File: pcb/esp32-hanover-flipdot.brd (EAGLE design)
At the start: 45.1 x 25.4 mm, 28 parts, among them J1 DC-005, J2 HANOVER, J3 FTDI, Q1 NCE3407A, Q2 S9013, U1 ESP32-PICO-D4, U2 CJA1117B-3.3-SOT89, U3 LM2576SX-5.0/NOPB

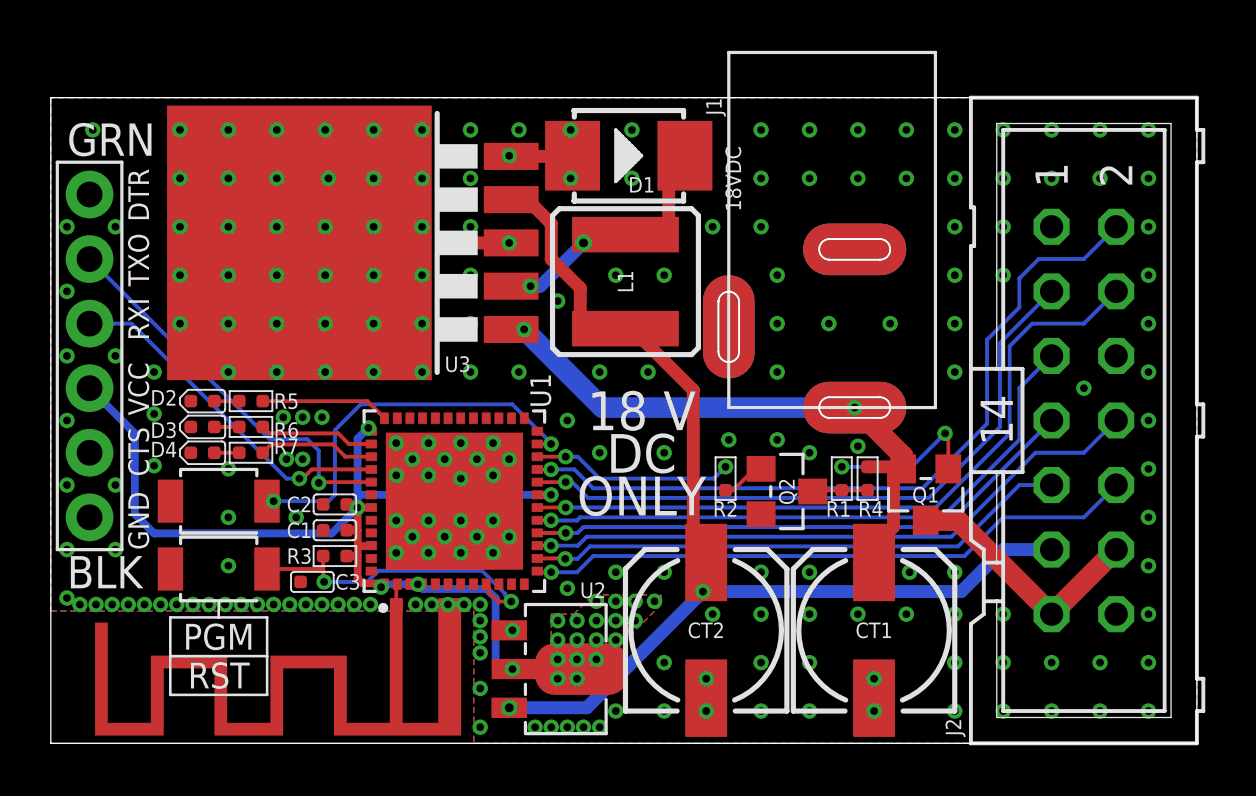
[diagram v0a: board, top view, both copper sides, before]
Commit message: pcb: Connect dot board pin 14 to COIL_PULSE (pin 12, pin 13) too
The 18V supply on this pin doesn't seem to be used, as it's wired to column darlington arrays while the dot boards seem to use the row darlingtons to source/sink. In any case, it should be safe to connect, tested splicing pin 12+13+14 together on a real dot board and it worked fine.
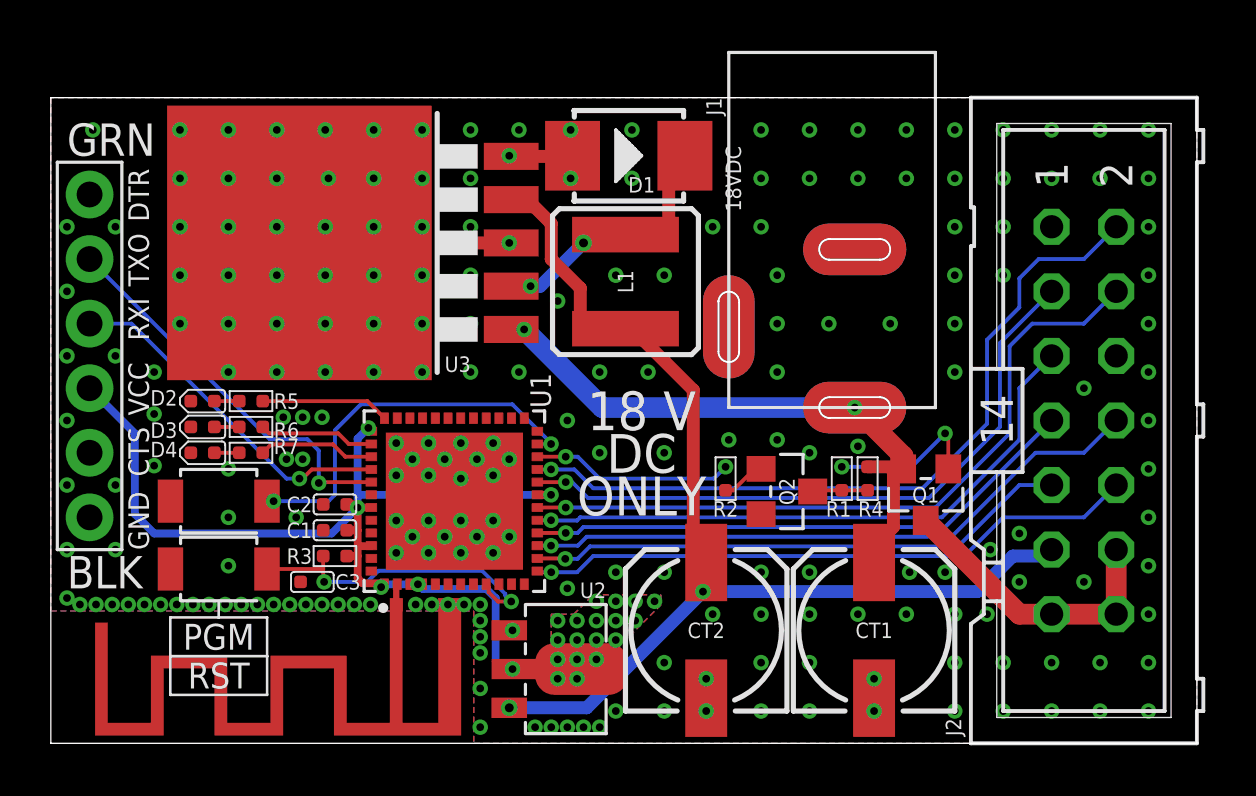
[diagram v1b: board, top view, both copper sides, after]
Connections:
- net COIL_PULSE: now also J2.14
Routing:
- net COIL_PULSE: track 10.1 -> 11.6 mm
- net +18V: track 23.4 -> 23.9 mm
- net GND: vias 220 -> 224
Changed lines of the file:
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@@
 <layers>
 <layer number="1" name="Top" color="4" fill="1" visible="yes" active="yes"/>
-<layer number="2" name="Route2" color="21" fill="1" visible="no" active="yes"/>
-<layer number="3" name="Route3" color="4" fill="3" visible="no" active="yes"/>
-<layer number="4" name="Route4" color="1" fill="4" visible="no" active="yes"/>
-<layer number="5" name="Route5" color="4" fill="4" visible="no" active="yes"/>
-<layer number="6" name="Route6" color="1" fill="8" visible="no" active="yes"/>
-<layer number="7" name="Route7" color="4" fill="8" visible="no" active="yes"/>
-<layer number="8" name="Route8" color="1" fill="2" visible="no" active="yes"/>
-<layer number="9" name="Route9" color="4" fill="2" visible="no" active="yes"/>
-<layer number="10" name="Route10" color="1" fill="7" visible="no" active="yes"/>
-<layer number="11" name="Route11" color="4" fill="7" visible="no" active="yes"/>
-<layer number="12" name="Route12" color="1" fill="5" visible="no" active="yes"/>
-<layer number="13" name="Route13" color="4" fill="5" visible="no" active="yes"/>
-<layer number="14" name="Route14" color="1" fill="6" visible="no" active="yes"/>
-<layer number="15" name="Route15" color="19" fill="1" visible="no" active="yes"/>
-<layer number="16" name="Bottom" color="1" fill="1" visible="no" active="yes"/>
+<layer number="2" name="Route2" color="21" fill="1" visible="yes" active="yes"/>
+<layer number="3" name="Route3" color="4" fill="3" visible="yes" active="yes"/>
+<layer number="4" name="Route4" color="1" fill="4" visible="yes" active="yes"/>
+<layer number="5" name="Route5" color="4" fill="4" visible="yes" active="yes"/>
+<layer number="6" name="Route6" color="1" fill="8" visible="yes" active="yes"/>
+<layer number="7" name="Route7" color="4" fill="8" visible="yes" active="yes"/>
+<layer number="8" name="Route8" color="1" fill="2" visible="yes" active="yes"/>
+<layer number="9" name="Route9" color="4" fill="2" visible="yes" active="yes"/>
+<layer number="10" name="Route10" color="1" fill="7" visible="yes" active="yes"/>
+<layer number="11" name="Route11" color="4" fill="7" visible="yes" active="yes"/>
+<layer number="12" name="Route12" color="1" fill="5" visible="yes" active="yes"/>
+<layer number="13" name="Route13" color="4" fill="5" visible="yes" active="yes"/>
+<layer number="14" name="Route14" color="1" fill="6" visible="yes" active="yes"/>
+<layer number="15" name="Route15" color="19" fill="1" visible="yes" active="yes"/>
+<layer number="16" name="Bottom" color="1" fill="1" visible="yes" active="yes"/>
 <layer number="17" name="Pads" color="2" fill="1" visible="yes" active="yes"/>
 <layer number="18" name="Vias" color="2" fill="1" visible="yes" active="yes"/>
@@
 <layer number="20" name="Dimension" color="15" fill="1" visible="yes" active="yes"/>
 <layer number="21" name="tPlace" color="16" fill="1" visible="yes" active="yes"/>
-<layer number="22" name="bPlace" color="14" fill="1" visible="no" active="yes"/>
+<layer number="22" name="bPlace" color="14" fill="1" visible="yes" active="yes"/>
 <layer number="23" name="tOrigins" color="15" fill="1" visible="yes" active="yes"/>
-<layer number="24" name="bOrigins" color="15" fill="1" visible="no" active="yes"/>
+<layer number="24" name="bOrigins" color="15" fill="1" visible="yes" active="yes"/>
 <layer number="25" name="tNames" color="7" fill="1" visible="yes" active="yes"/>
-<layer number="26" name="bNames" color="7" fill="1" visible="no" active="yes"/>
+<layer number="26" name="bNames" color="7" fill="1" visible="yes" active="yes"/>
 <layer number="27" name="tValues" color="7" fill="1" visible="no" active="yes"/>
 <layer number="28" name="bValues" color="7" fill="1" visible="no" active="yes"/>
@@
 <layer number="38" name="bTest" color="7" fill="1" visible="no" active="yes"/>
 <layer number="39" name="tKeepout" color="4" fill="11" visible="yes" active="yes"/>
-<layer number="40" name="bKeepout" color="1" fill="11" visible="no" active="yes"/>
+<layer number="40" name="bKeepout" color="1" fill="11" visible="yes" active="yes"/>
 <layer number="41" name="tRestrict" color="4" fill="10" visible="yes" active="yes"/>
-<layer number="42" name="bRestrict" color="1" fill="10" visible="no" active="yes"/>
+<layer number="42" name="bRestrict" color="1" fill="10" visible="yes" active="yes"/>
 <layer number="43" name="vRestrict" color="2" fill="10" visible="no" active="yes"/>
 <layer number="44" name="Drills" color="7" fill="1" visible="no" active="yes"/>
@@
 <layer number="50" name="dxf" color="7" fill="1" visible="no" active="yes"/>
 <layer number="51" name="tDocu" color="6" fill="1" visible="yes" active="yes"/>
-<layer number="52" name="bDocu" color="7" fill="1" visible="no" active="yes"/>
+<layer number="52" name="bDocu" color="7" fill="1" visible="yes" active="yes"/>
 <layer number="91" name="Nets" color="2" fill="1" visible="no" active="no"/>
 <layer number="92" name="Busses" color="1" fill="1" visible="no" active="no"/>
@@
 <element name="D1" library="OPL_Discrete_Semiconductor" library_urn="urn:adsk.eagle:library:8004488" package="DO-214AA" package3d_urn="urn:adsk.eagle:package:8004541/1" value="28V-5A" x="22.733" y="23.114" smashed="yes">
 <attribute name="MPN" value="SS54B" x="22.733" y="23.114" size="1.778" layer="27" display="off"/>
+<attribute name="NAME" x="23.241" y="21.971" size="0.6096" layer="25" ratio="11" align="center"/>
 <attribute name="NAME" x="24.003" y="23.114" size="0.5" layer="33" ratio="10" rot="R180"/>
-<attribute name="NAME" x="23.241" y="21.971" size="0.6096" layer="25" ratio="11" align="center"/>
 <attribute name="VALUE" x="21.082" y="20.32" size="0.635" layer="27" ratio="10"/>
 </element>
@@
 <via x="27.94" y="6.731" extent="1-16" drill="0.3048"/>
 <via x="29.845" y="6.731" extent="1-16" drill="0.3048"/>
-<via x="35.56" y="6.731" extent="1-16" drill="0.3048"/>
 <via x="28.575" y="11.938" extent="1-16" drill="0.3048"/>
 <via x="26.67" y="11.938" extent="1-16" drill="0.3048"/>
@@
 <via x="18.034" y="23.114" extent="1-16" drill="0.3048"/>
 <via x="19.939" y="17.399" extent="1-16" drill="0.3048"/>
-<via x="33.782" y="6.731" extent="1-16" drill="0.3048"/>
+<via x="35.179" y="6.731" extent="1-16" drill="0.3048"/>
 <via x="33.655" y="5.08" extent="1-16" drill="0.3048"/>
 <via x="35.56" y="5.08" extent="1-16" drill="0.3048"/>
-<via x="37.465" y="5.08" extent="1-16" drill="0.3048"/>
 <via x="32.385" y="1.27" extent="1-16" drill="0.3048"/>
 <via x="32.385" y="2.54" extent="1-16" drill="0.3048"/>
@@
 <via x="0.635" y="7.62" extent="1-16" drill="0.3048"/>
 <via x="2.54" y="7.62" extent="1-16" drill="0.3048"/>
+<via x="40.64" y="6.35" extent="1-16" drill="0.3048"/>
+<via x="38.1" y="6.35" extent="1-16" drill="0.3048"/>
+<via x="38.1" y="8.255" extent="1-16" drill="0.3048"/>
+<via x="36.957" y="7.62" extent="1-16" drill="0.3048"/>
+<via x="33.782" y="6.731" extent="1-16" drill="0.3048"/>
+<via x="36.83" y="5.08" extent="1-16" drill="0.3048"/>
 </signal>
 <signal name="ANT">
 <contactref element="U1" pad="2"/>
 <contactref element="E1" pad="ANT"/>
-<wire x1="13.589" y1="6.26" x2="13.589" y2="5.457" width="0.1524" layer="1"/>
+<wire x1="13.589" y1="6.26" x2="13.589" y2="5.457" width="0.254" layer="1"/>
 <wire x1="13.625" y1="6.26" x2="13.589" y2="6.26" width="0.1524" layer="1"/>
 </signal>
@@
 <via x="31.623" y="13.208" extent="1-16" drill="0.3048"/>
 <wire x1="21.6916" y1="13.208" x2="31.623" y2="13.208" width="0.8128" layer="16"/>
-<wire x1="18.6182" y1="16.2814" x2="18.1102" y2="16.2814" width="0" layer="19" extent="1-1"/>
+<wire x1="18.1102" y1="16.2814" x2="18.6182" y2="16.2814" width="0.8128" layer="1"/>
 </signal>
 <signal name="COIL_PULSE">
@@
 <contactref element="Q1" pad="3"/>
 <contactref element="J2" pad="13"/>
-<wire x1="34.417" y1="8.763" x2="35.687" y2="8.763" width="0.8128" layer="1"/>
-<wire x1="39.37" y1="5.08" x2="35.687" y2="8.763" width="0.8128" layer="1"/>
-<wire x1="39.37" y1="5.08" x2="41.91" y2="7.62" width="0.8128" layer="1"/>
+<wire x1="39.37" y1="5.08" x2="38.1" y2="5.08" width="0.8128" layer="1"/>
+<wire x1="38.1" y1="5.08" x2="34.417" y2="8.763" width="0.8128" layer="1"/>
+<contactref element="J2" pad="14"/>
+<wire x1="41.91" y1="7.62" x2="41.91" y2="5.08" width="0.8128" layer="1"/>
+<wire x1="39.37" y1="5.08" x2="41.91" y2="5.08" width="0.8128" layer="1"/>
 </signal>
 <signal name="+5V" class="1">
@@
 <via x="25.654" y="5.969" extent="1-16" drill="0.3048"/>
 <wire x1="21.082" y1="1.397" x2="25.654" y2="5.969" width="0.508" layer="16"/>
-<wire x1="35.814" y1="5.969" x2="25.654" y2="5.969" width="0.508" layer="16"/>
-<wire x1="37.465" y1="7.62" x2="39.37" y2="7.62" width="0.508" layer="16"/>
-<wire x1="37.465" y1="7.62" x2="35.814" y2="5.969" width="0.508" layer="16"/>
+<wire x1="36.449" y1="5.969" x2="25.654" y2="5.969" width="0.508" layer="16"/>
+<wire x1="39.116" y1="7.366" x2="39.37" y2="7.62" width="0.508" layer="16"/>
+<wire x1="39.116" y1="7.366" x2="37.846" y2="7.366" width="0.508" layer="16"/>
+<wire x1="37.846" y1="7.366" x2="36.449" y2="5.969" width="0.508" layer="16"/>
 <wire x1="25.781" y1="7.112" x2="25.781" y2="6.985" width="0.3048" layer="1"/>
 <wire x1="25.781" y1="6.985" x2="25.781" y2="6.096" width="0.508" layer="1"/>
